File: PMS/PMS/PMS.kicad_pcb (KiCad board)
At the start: 4 copper layers, 97.5 x 67.5 mm, 34 parts, among them IC1 TMCS1107A1BQDRQ1, J1 XT90PW-M, J2 OSTYK44105030, J4 XT60PW-F, J5 XT90PWM, J6 Conn_01x03_Male, J7 Conn_01x02_Male, U1 ADC101C027CIMK, U2 ADC101C027CIMK, U4 REF195

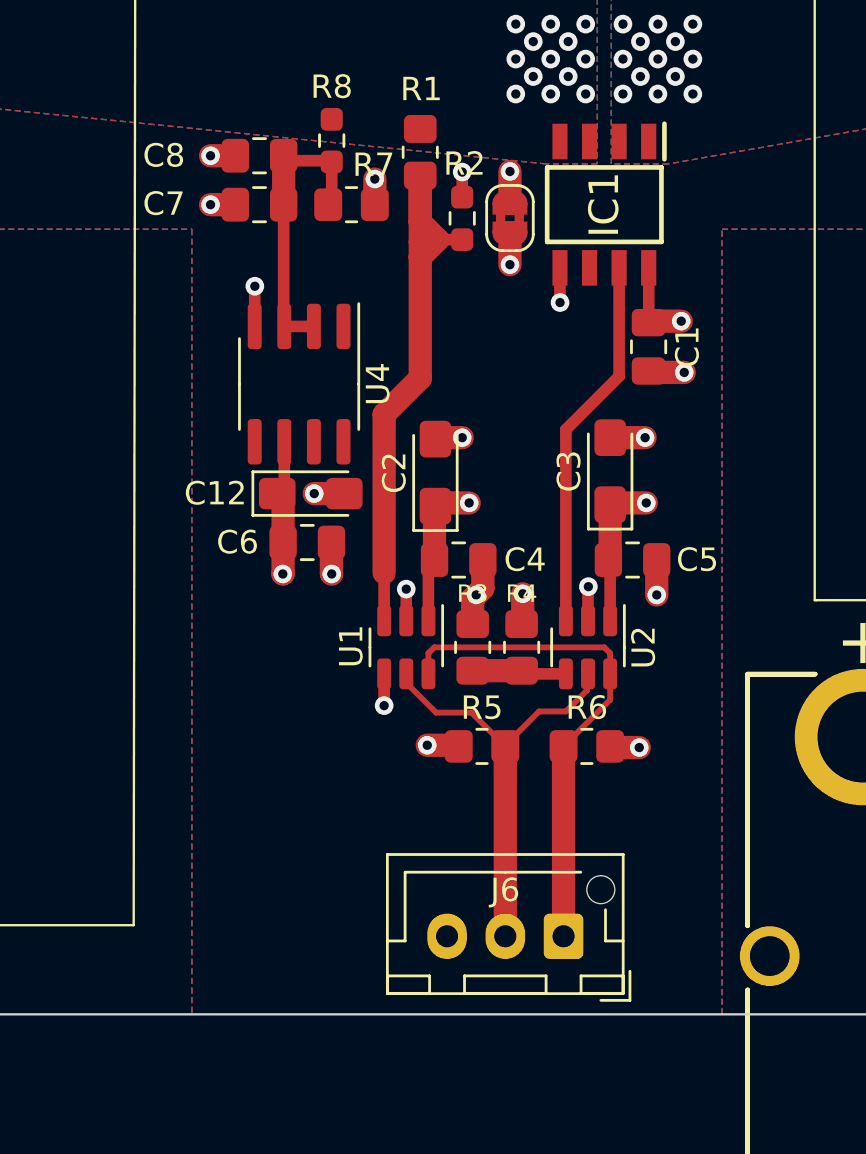
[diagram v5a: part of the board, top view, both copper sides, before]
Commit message: updated PMS. Resistor values chosen for accurate current. ADC layouts altered to add via fence and reduce EMI. ADC input low-pass capacitors added.
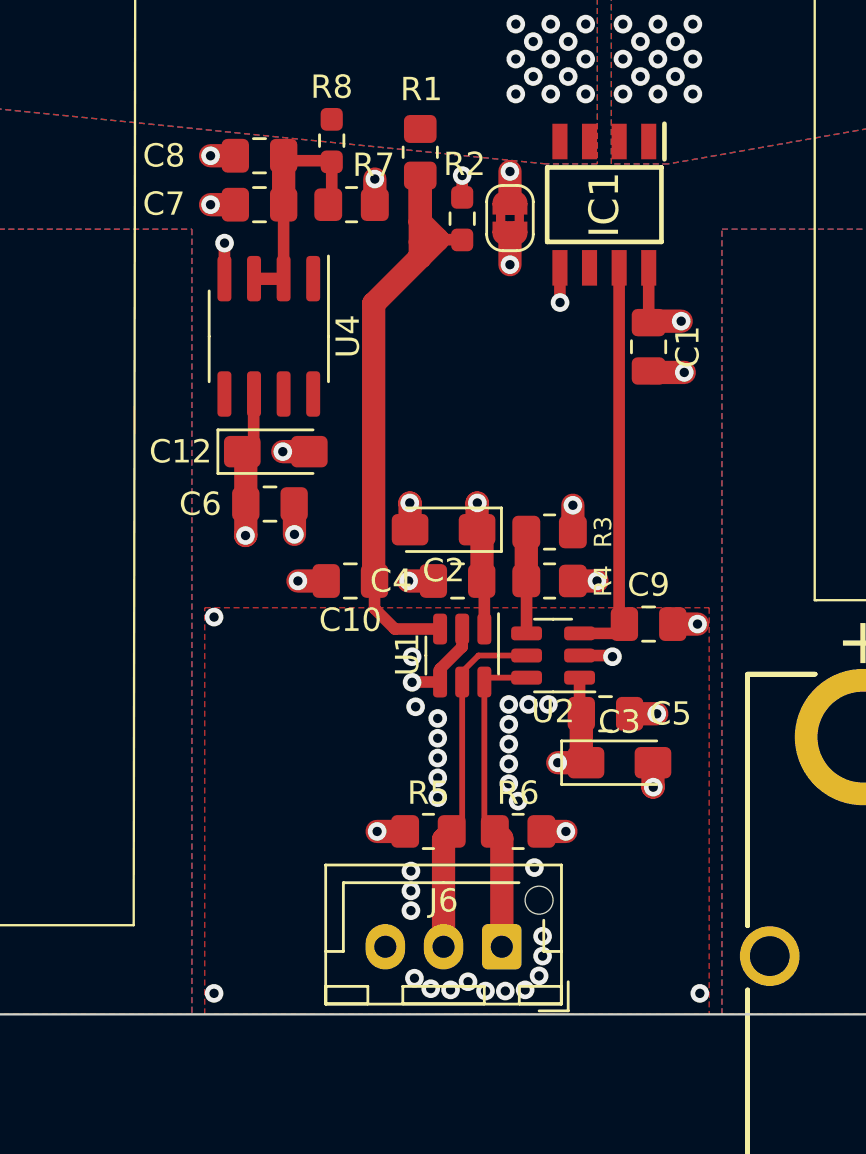
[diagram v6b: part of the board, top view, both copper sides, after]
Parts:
- added C10: 470 pF, Capacitor_SMD:C_0805_2012Metric_Pad1.18x1.45mm_HandSolder, F.Cu at (95.1, 89.7)
- added C9: 470 pF, Capacitor_SMD:C_0805_2012Metric_Pad1.18x1.45mm_HandSolder, F.Cu at (107.9, 91.5)
- J5: value XT90PWM -> XT90PW-F
- R1: value 10M -> 100K
- R2: value 2M -> 20K
- R7: value 1M -> 1.5K
- R8: value 2M -> 1.5K
- moved C3 12.5 mm to (106.7, 97.5), turned to 0 degrees
- moved C5 6.70 mm to (106.0, 95.3)
- moved R3 5.95 mm to (103.7, 87.5), turned to 0 degrees
- moved R6 4.69 mm to (102.3, 100.4)
- moved R5 4.31 mm to (98.5, 100.4)
- moved R4 3.09 mm to (103.7, 89.7), turned to 0 degrees
- moved J6 2.69 mm to (101.6, 105.3)
- moved C2 2.47 mm to (99.1, 87.5), turned to 180 degrees
- moved U4 2.43 mm to (91.6, 79.2)
- moved U1 2.43 mm to (99.9, 92.8)
- moved C12 2.34 mm to (91.9, 84.1)
- moved C6 2.30 mm to (91.7, 86.3)
- moved U2 1.54 mm to (103.8, 92.8), turned to 180 degrees
- moved C4 0.90 mm to (99.7, 89.7), turned to 180 degrees
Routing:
- net SDA: track 21.9 -> 13.6 mm
- net SCL: track 18.3 -> 15.2 mm
- net Net-(C10-Pad1): track 25.7 -> 28.6 mm
- net +5VA: track 25.6 -> 23.9 mm
- net GNDA: track 19.9 -> 21.4 mm, vias 13 -> 47
- net Net-(C9-Pad1): track 16.1 -> 17.5 mm
- net Net-(C7-Pad2): track 11.9 -> 11.1 mm
- net Net-(R3-Pad1): track 3.81 -> 4.36 mm
- added copper zone on F.Cu, net GNDA

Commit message: minor changes
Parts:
- removed JP1: Jumper_2_Bridged, Jumper:SolderJumper-2_P1.3mm_Bridged2Bar_RoundedPad1.0x1.5mm
- moved C10 2.35 mm to (96.2, 91.8)
- moved R2 2.19 mm to (101.5, 72.5), turned to 0 degrees
- moved C2 2.17 mm to (100.8, 86.0), turned to 90 degrees
- moved R1 0.30 mm to (98.1, 71.5)
- moved C3 0.25 mm to (106.7, 97.7)
- moved C5 0.25 mm to (106.0, 95.6)
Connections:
- C1 pad 2: GNDA -> GND
- C10 pad 2: GNDA -> GND
- C12 pad 2: GNDA -> GND
- C2 pad 2: GNDA -> GND
- C3 pad 2: GNDA -> GND
- C4 pad 2: GNDA -> GND
- C5 pad 2: GNDA -> GND
- C6 pad 2: GNDA -> GND
- C9 pad 2: GNDA -> GND
- IC1 pad 5: GNDA -> GND
- R3 pad 2: GNDA -> GND
- U1 pad 2: GNDA -> GND
- U1 pad 4: GNDA -> GND
- U2 pad 2: GNDA -> GND
- U4 pad 4: GNDA -> GND
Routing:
- net GNDA: track 21.4 -> 0.00 mm, vias 47 -> 0
- net GND: track 5.51 -> 25.9 mm, vias 5 -> 50
- net Net-(C10-Pad1): track 28.6 -> 23.7 mm
- net Net-(C7-Pad2): track 11.1 -> 9.73 mm
- net SCL: track 15.2 -> 14.1 mm
- net SDA: track 13.6 -> 12.9 mm
- net +5VA: track 23.9 -> 23.3 mm
- added copper zone on F.Cu, net GND
- removed copper zone on F.Cu, net GNDA
- removed copper zone on In1.Cu, net GNDA

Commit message: changed star ground
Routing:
- net GND: track 25.9 -> 24.1 mm
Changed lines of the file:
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@@
   (via (at 108.2 95.6) (size 0.8) (drill 0.4) (layers "F.Cu" "B.Cu") (net 2))
   (via (at 98.85 98.95) (size 0.8) (drill 0.4) (layers "F.Cu" "B.Cu") (free) (net 2))
-  (segment (start 92.25 73.8) (end 92.25 74.7) (width 1) (layer "In1.Cu") (net 2))
-  (segment (start 98.1 73.8) (end 98.1 74.7) (width 1) (layer "In1.Cu") (net 2))
   (via (at 108.3 65.75) (size 0.8) (drill 0.4) (layers "F.Cu" "B.Cu") (free) (net 4))
   (via (at 108.3 68.75) (size 0.8) (drill 0.4) (layers "F.Cu" "B.Cu") (free) (net 4))
@@
         (xy 111.05 108.25)
         (xy 111.05 74)
+        (xy 108.75 74)
+        (xy 108.75 74.55)
+        (xy 91.2 74.55)
+        (xy 91.2 74)
         (xy 88.3 74)
         (xy 88.3 108.25)
